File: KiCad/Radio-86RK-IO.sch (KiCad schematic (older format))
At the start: 16 parts, among them J5 Serial, J6 Parallel, Q2 2N3904, U16 7486/К155ЛП5, U20 7400/К155ЛА3, U22 SN75154N/К170УП2В, U23 SN75150P/К170АП2, U24 SN75150P/К170АП2, U3 8251A/КР580ВВ51А, U4 8253/КР580ВИ53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

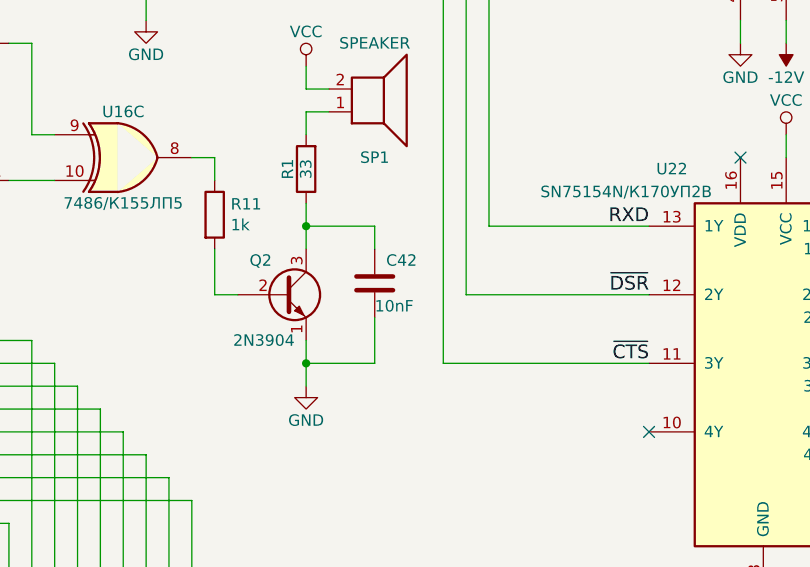
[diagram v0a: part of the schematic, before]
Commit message: Update design files to v1.1
Signed-off-by: Sergey Kiselev <skiselev@gmail.com>
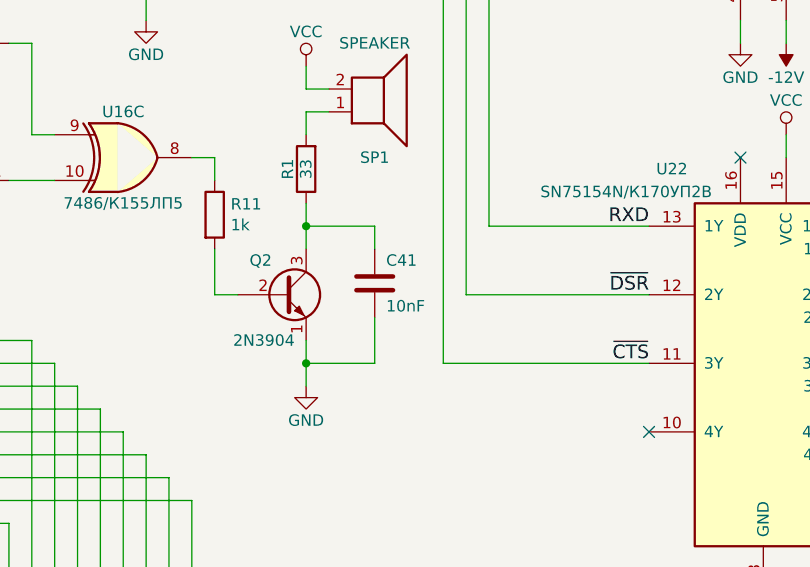
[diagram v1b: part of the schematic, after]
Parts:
- renumbered C42 to C41
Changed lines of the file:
@@
 	6800 4800 7100 4800
 $Comp
-L Device:C C42
+L Device:C C41
 U 1 1 600E6B82
 P 7100 4450
-F 0 "C42" H 7150 4550 50  0000 L CNN
-F 1 "10nF" H 7100 4350 50  0000 L CNN
+F 0 "C41" H 7150 4550 50  0000 L CNN
+F 1 "10nF" H 7150 4350 50  0000 L CNN
 F 2 "My_Components:Cap_Cer_508" H 7138 4300 50  0001 C CNN
 F 3 "~" H 7100 4450 50  0001 C CNN
